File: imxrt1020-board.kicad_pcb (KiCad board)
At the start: 2 copper layers, 102.9 x 68.6 mm, 200 parts, among them J1 Micro_SD_Card_Det, J10 CASTELATED, J11 CASTELATED, J12 CASTELATED, J13 CASTELATED, J14 CASTELATED, J15 CASTELATED, J16 CASTELATED, J17 CASTELATED, J18 CASTELATED, J19 CASTELATED, J2 USB_OTG, J20 CASTELATED, J21 CASTELATED, J22 CASTELATED, J23 CASTELATED, J24 CASTELATED, J25 CASTELATED, J26 CASTELATED, J27 CASTELATED, J28 CASTELATED, J29 CASTELATED, J3 Conn_02x20_Odd_Even, J30 CASTELATED, J31 CASTELATED, J32 CASTELATED, J33 CASTELATED, J34 CASTELATED, J35 CASTELATED, J36 CASTELATED, J37 CASTELATED, J38 CASTELATED, J39 CASTELATED, J4 CASTELATED, J40 CASTELATED, J41 CASTELATED, J42 CASTELATED, J43 CASTELATED, J44 GS2, J45 GS2, J46 PWR_IN, J47 JTAG, J48 Conn_01x06, J49 CASTELATED, J5 CASTELATED, J50 CASTELATED, J51 CASTELATED, J52 CASTELATED, J53 CASTELATED, J54 CASTELATED, J55 CASTELATED, J56 CASTELATED, J57 CASTELATED, J58 SI-50196-F, J59 CASTELATED, J6 CASTELATED, J60 CASTELATED, J61 CASTELATED, J62 CASTELATED, J63 CASTELATED, J64 CASTELATED, J65 CASTELATED, J66 CASTELATED, J67 CASTELATED, J68 CASTELATED, J69 CASTELATED, J7 CASTELATED, J70 CASTELATED, J71 CASTELATED, J72 CASTELATED, J73 CASTELATED, J74 CASTELATED, J75 CASTELATED, J76 CASTELATED, J77 CASTELATED, J78 CASTELATED, J79 CASTELATED, J8 CASTELATED, J80 CASTELATED, J81 Conn_01x07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

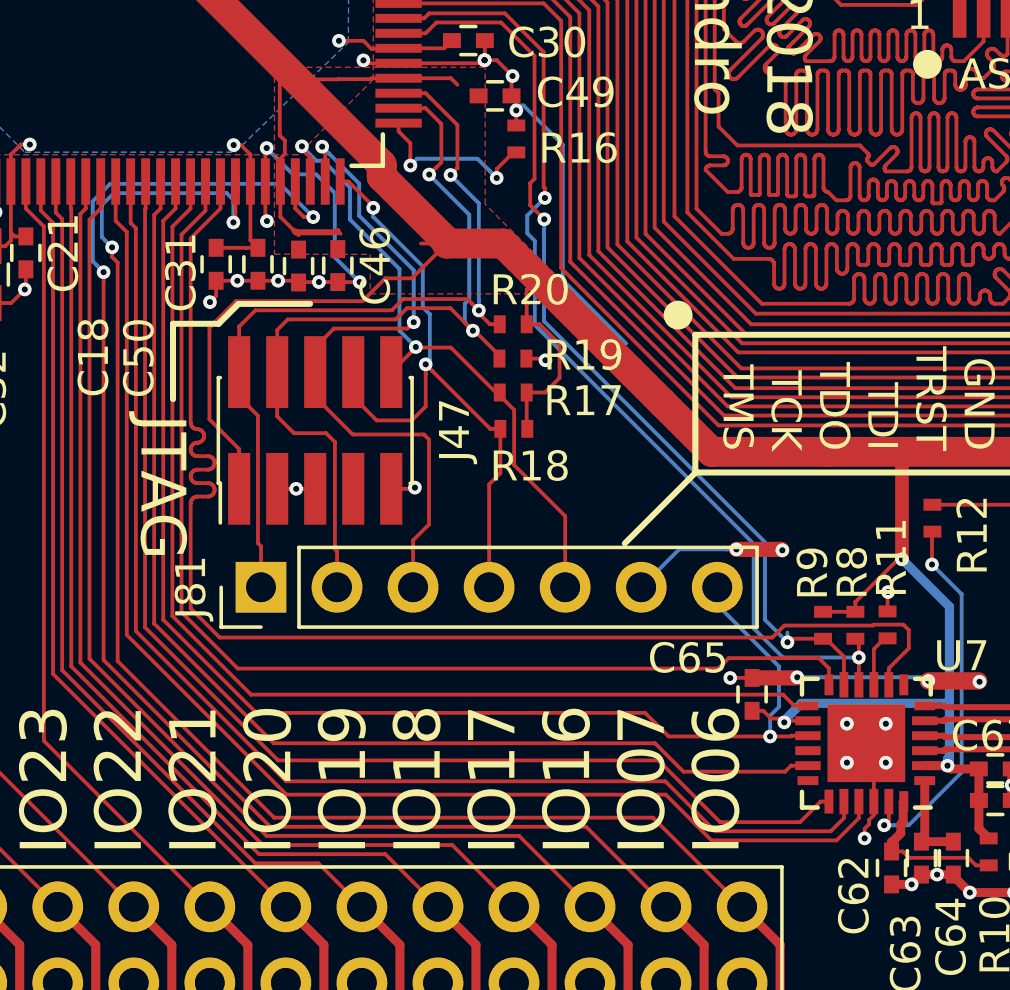
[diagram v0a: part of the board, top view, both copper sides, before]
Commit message: Tune track length of ETH data lines
Signed-off-by: Martin Ribelotta <martinribelotta@gmail.com>
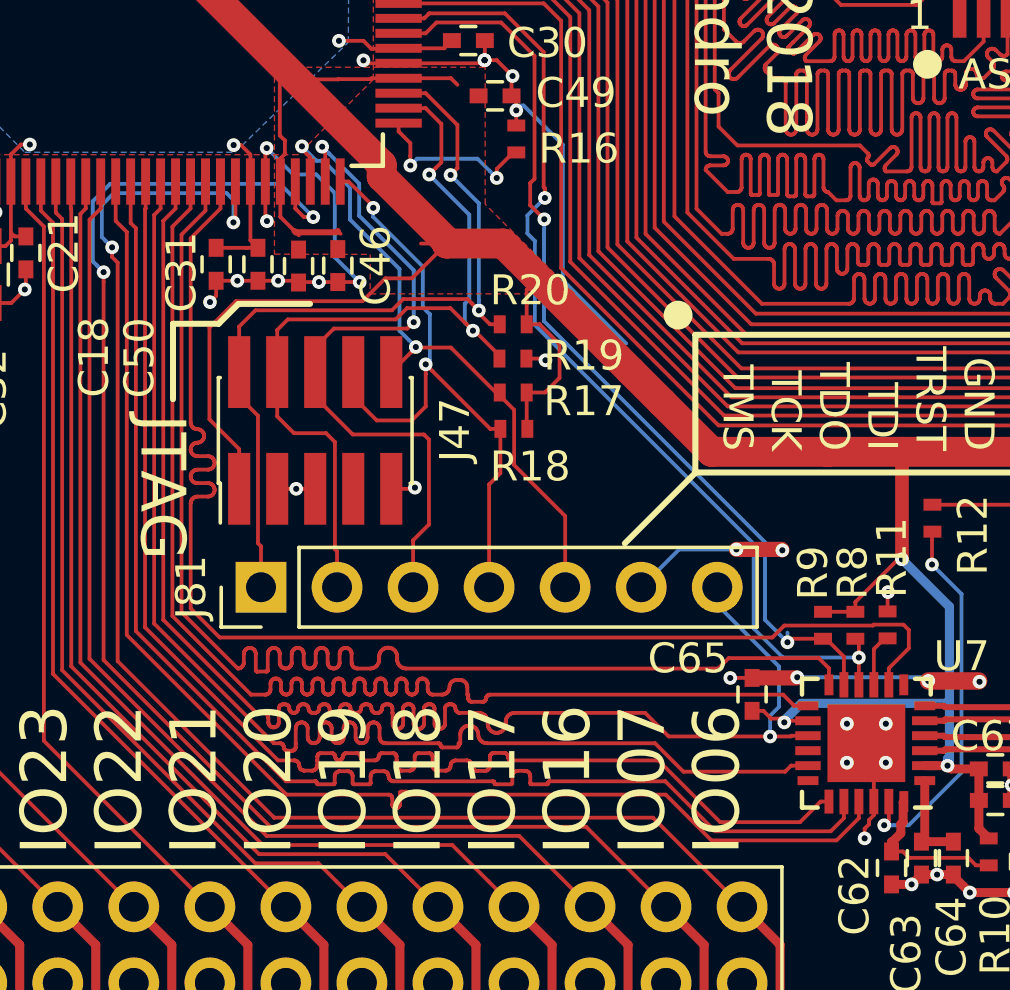
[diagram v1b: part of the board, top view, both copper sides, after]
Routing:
- net /GPIO/ENET_CRS_DV: track 43.9 -> 51.6 mm
- net /GPIO/ENET_RXD0: track 37.2 -> 44.4 mm
- net /GPIO/ENET_RXD1: track 38.0 -> 44.4 mm
- net /GPIO/ENET_RX_ER: track 38.8 -> 44.4 mm
- net /GPIO/ENET_TX_EN: track 40.7 -> 44.3 mm
- net /GPIO/ENET_TXD0: track 42.2 -> 44.3 mm
- net /GPIO/ENET_TXD1: track 43.5 -> 44.3 mm

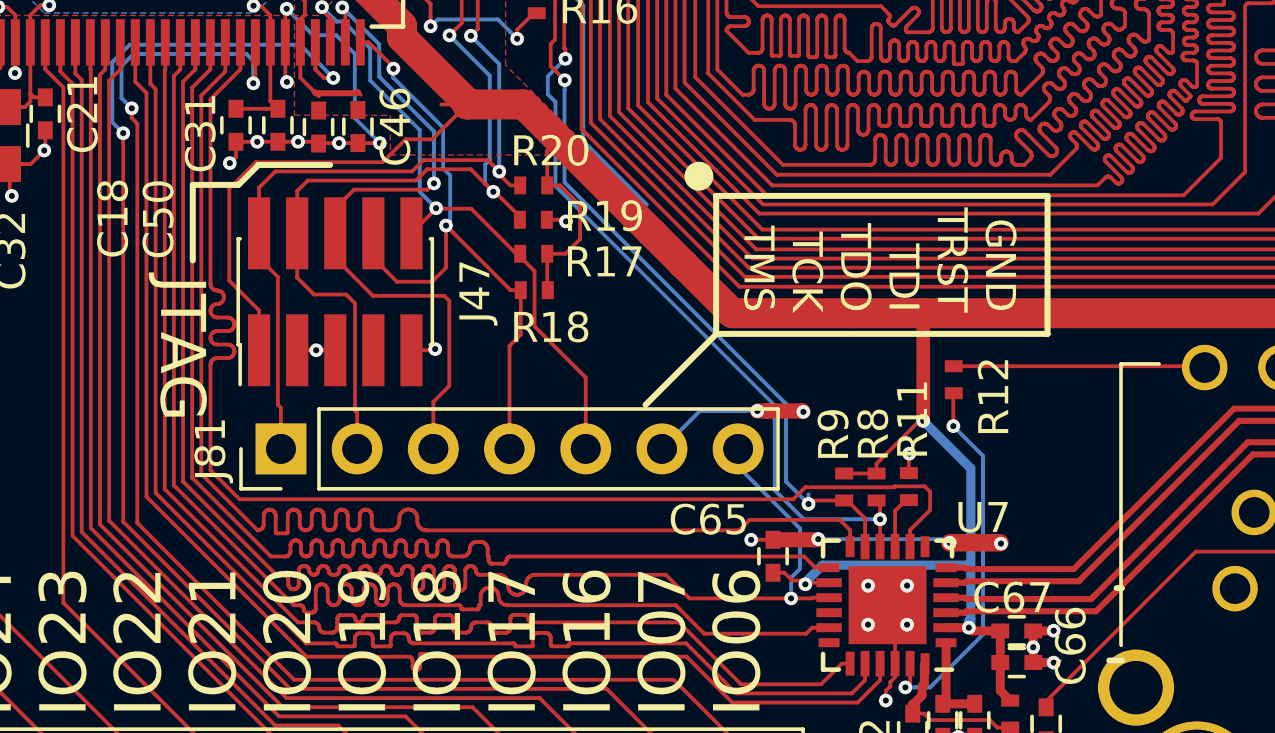
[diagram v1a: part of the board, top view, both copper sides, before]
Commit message: Update images, README.md and PCB sylkscreen for reflect the changes
Signed-off-by: Martin Ribelotta <martinribelotta@gmail.com>
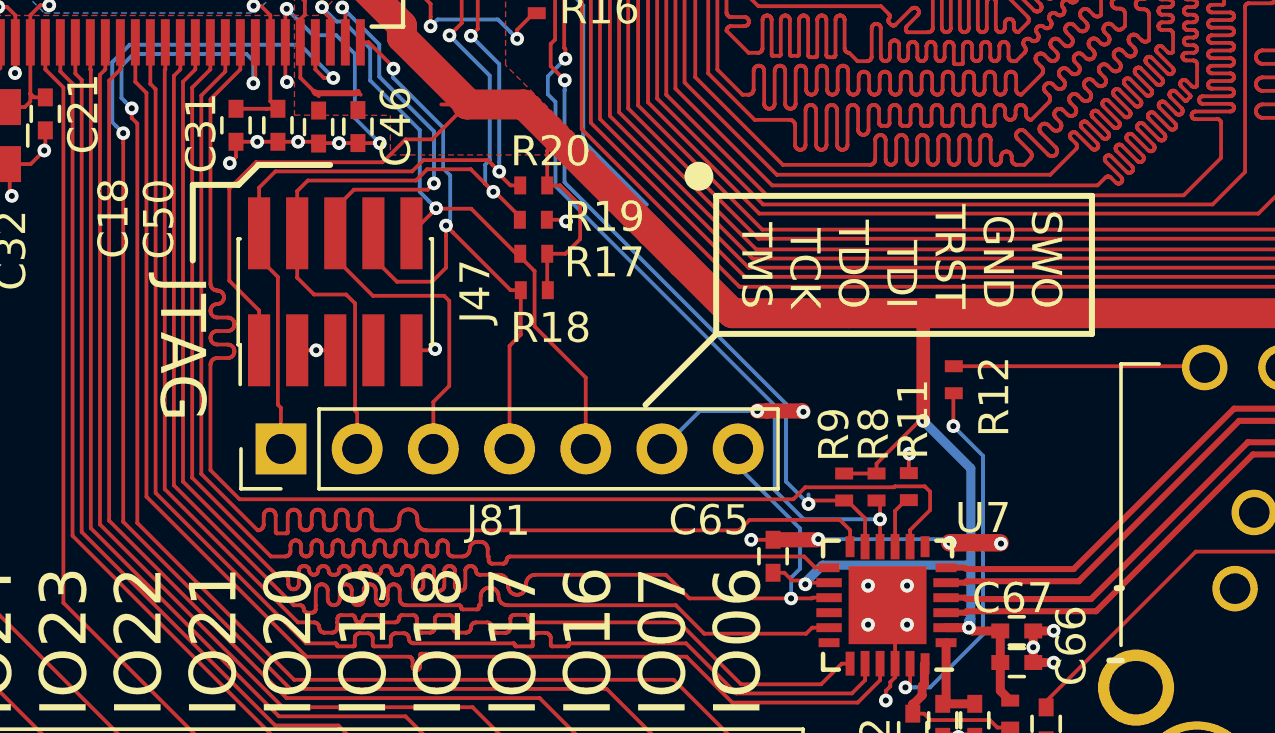
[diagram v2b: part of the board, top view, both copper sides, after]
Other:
- board text added: "SWO GND TRST TDI TDO TCK TMS"
- board text removed: "GND TRST TDI TDO TCK TMS"
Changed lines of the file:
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@@
     (descr "Through hole straight pin header, 1x07, 2.54mm pitch, single row")
     (tags "Through hole pin header THT 1x07 2.54mm single row")
-    (fp_text reference J81 (at 0 -2.33 90) (layer F.SilkS)
+    (fp_text reference J81 (at -2.4003 7.24662 180) (layer F.SilkS)
       (effects (font (size 1 1) (thickness 0.15)))
     )
@@
     (pad 7 thru_hole oval (at 0 15.24 90) (size 1.7 1.7) (drill 1) (layers *.Cu *.Mask)
       (net 87 /GPIO/ENET_CRS_DV))
-    (model ${KISYS3DMOD}/Pin_Headers.3dshapes/Pin_Header_Straight_1x07_Pitch2.54mm.wrl
-      (at (xyz 0 0 0))
-      (scale (xyz 1 1 1))
-      (rotate (xyz 0 0 0))
-    )
   )
   (gr_line (start 198.98868 81.26476) (end 206.68996 81.26476) (layer F.SilkS) (width 0.2))
@@
   (gr_line (start 174.79772 120.2436) (end 172.43298 122.60834) (layer F.SilkS) (width 0.2))
   (gr_circle (center 174.21352 114.984276) (end 174.35322 115.169696) (layer F.SilkS) (width 0.5))
-  (gr_line (start 185.83402 115.64112) (end 174.79264 115.64112) (layer F.SilkS) (width 0.2))
-  (gr_line (start 185.83402 120.24106) (end 185.83402 115.64112) (layer F.SilkS) (width 0.2))
-  (gr_line (start 174.7901 120.24106) (end 185.83402 120.24106) (layer F.SilkS) (width 0.2))
+  (gr_line (start 187.31484 115.64112) (end 174.79264 115.64112) (layer F.SilkS) (width 0.2))
+  (gr_line (start 187.31484 120.24106) (end 187.31484 115.64112) (layer F.SilkS) (width 0.2))
+  (gr_line (start 174.7901 120.24106) (end 187.31484 120.24106) (layer F.SilkS) (width 0.2))
   (gr_line (start 174.7901 115.64112) (end 174.7901 120.24106) (layer F.SilkS) (width 0.2))
-  (gr_text "GND\nTRST\nTDI\nTDO\nTCK\nTMS" (at 180.22316 119.52478 270) (layer F.SilkS)
+  (gr_text "SWO\nGND\nTRST\nTDI\nTDO\nTCK\nTMS" (at 180.95468 119.41048 270) (layer F.SilkS)
     (effects (font (size 1 1) (thickness 0.25)) (justify right))
   )

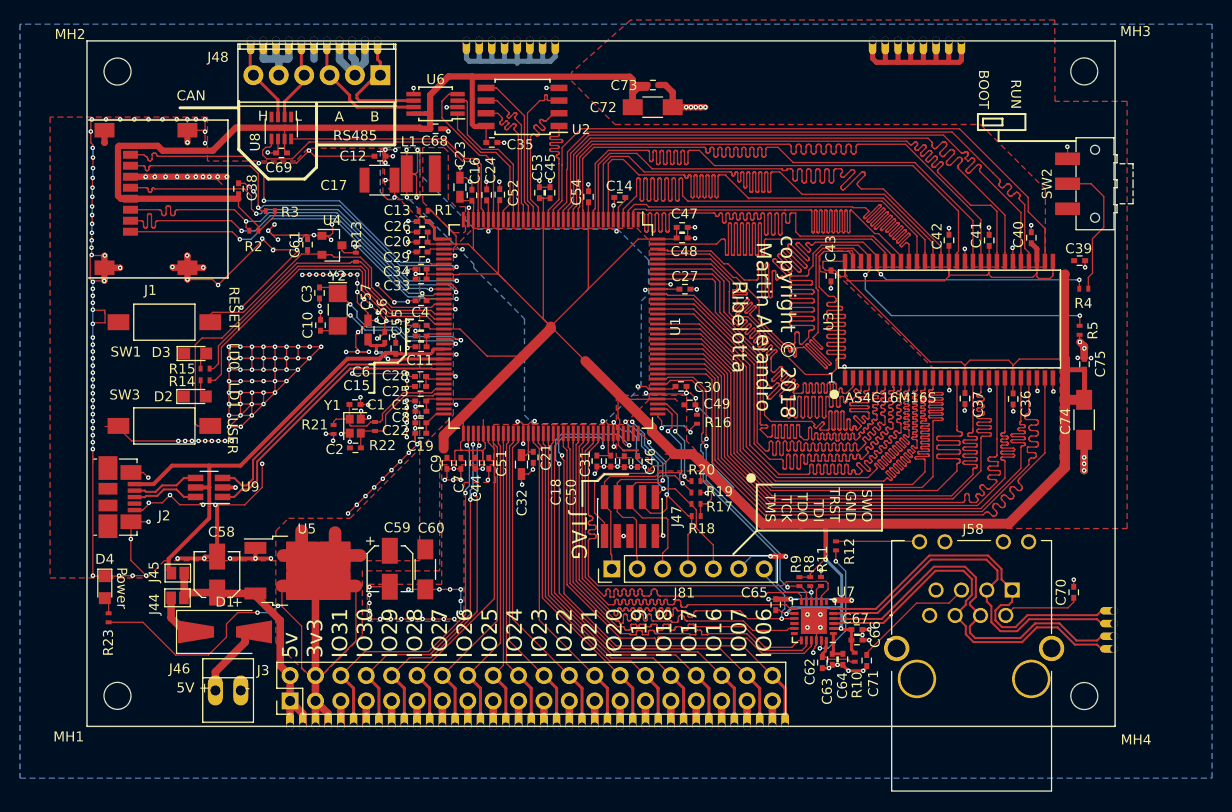
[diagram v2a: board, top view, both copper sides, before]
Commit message: First route of 6mil/6mil experiment
Signed-off-by: Martin Ribelotta <martinribelotta@gmail.com>
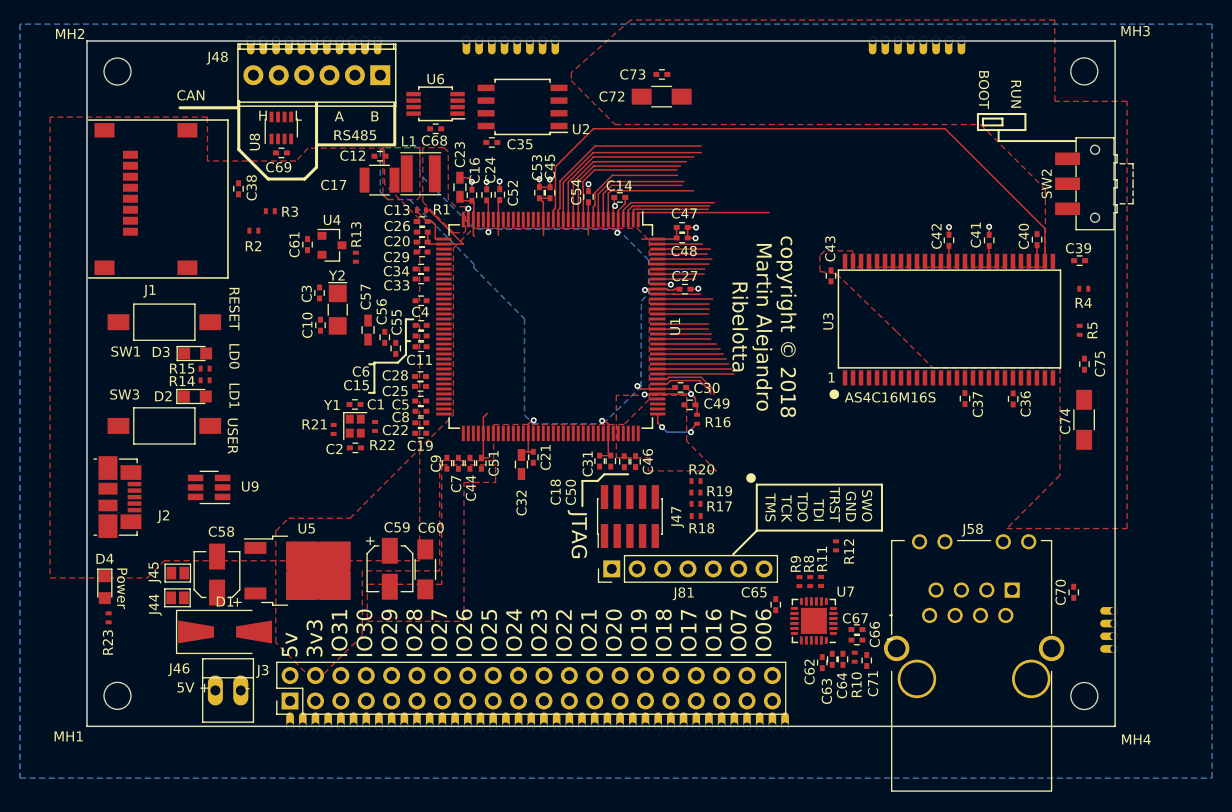
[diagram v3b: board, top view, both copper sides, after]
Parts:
- moved C72 1.38 mm to (165.3, 76.8)
- moved C73 1.38 mm to (165.3, 74.6)
- moved C51 0.75 mm to (147.2, 113.5)
- moved C40 0.60 mm to (202.8, 91.1)
- moved C44 0.49 mm to (146.1, 113.5)
- moved C31 0.28 mm to (159.1, 113.3)
- moved C7 0.25 mm to (144.9, 113.5)
- moved C46 0.19 mm to (162.7, 113.3)
- moved R1 0.18 mm to (141.2, 88.2)
- moved C30 0.11 mm to (167.2, 105.9)
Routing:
- net GND: track 620.8 -> 24.8 mm, vias 336 -> 16
- net +3V3: track 600.7 -> 41.1 mm, vias 7 -> 0
- net /MEMORY/SDRAM_A1: track 91.5 -> 4.96 mm, vias 2 -> 0
- net /MEMORY/SDRAM_A0: track 87.4 -> 5.27 mm, vias 2 -> 0
- net /MEMORY/SDRAM_A6: track 64.9 -> 3.74 mm
- net /MEMORY/SDRAM_A7: track 64.9 -> 4.30 mm
- net /MEMORY/SDRAM_A10: track 64.9 -> 4.46 mm
- net /MEMORY/SDRAM_A5: track 64.9 -> 4.64 mm
- net /MEMORY/SDRAM_A4: track 64.9 -> 4.72 mm
- net /MEMORY/SDRAM_CLK: track 64.9 -> 5.07 mm
- net /MEMORY/SDRAM_CKE: track 64.9 -> 5.08 mm
- net /MEMORY/SDRAM_A12: track 64.9 -> 5.08 mm
- net /MEMORY/SDRAM_A9: track 64.9 -> 5.15 mm
- net /MEMORY/SDRAM_A11: track 64.9 -> 5.15 mm
- net /MEMORY/SDRAM_Q8: track 64.9 -> 5.31 mm
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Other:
- net class Default: trace_width 0.127 -> 0.1524; via_dia 0.4572 -> 0.6; via_drill 0.2032 -> 0.3
- rule trace_min: 0.127 -> 0.1524
- rule via_min_drill: 0.2032 -> 0.3
- rule via_min_size: 0.4572 -> 0.6

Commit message: Save commit after kicad-5 migration
Signed-off-by: Martin Ribelotta <martinribelotta@gmail.com>
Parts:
- moved R5 23.0 mm to (186.0, 91.2), turned to 90 degrees
- moved R2 2.38 mm to (124.6, 87.9), turned to 0 degrees
- moved R3 2.28 mm to (124.5, 86.6), turned to 0 degrees
- moved R22 0.57 mm to (137.1, 109.5)
- moved C16 0.24 mm to (146.3, 86.4)
- moved C23 0.24 mm to (145.1, 85.6)
- moved C43 0.08 mm to (182.1, 94.7)
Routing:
- net /MEMORY/SDRAM_CLK: track 5.07 -> 61.2 mm
- net /MEMORY/SDRAM_A12: track 5.08 -> 61.1 mm
- net /MEMORY/SDRAM_CKE: track 5.08 -> 61.1 mm
- net /MEMORY/SDRAM_A11: track 5.15 -> 61.1 mm
- net /MEMORY/SDRAM_Q15: track 7.63 -> 55.3 mm
- net /MEMORY/SDRAM_Q14: track 7.36 -> 54.0 mm
- net /MEMORY/SDRAM_Q13: track 7.10 -> 53.1 mm
- net /MEMORY/SDRAM_A0: track 5.27 -> 49.9 mm, vias 0 -> 2
- net /MEMORY/SDRAM_Q12: track 6.85 -> 51.2 mm
- net GND: track 24.8 -> 69.0 mm, vias 16 -> 57
- net /MEMORY/SDRAM_Q11: track 6.56 -> 50.2 mm
- net /MEMORY/SDRAM_Q10: track 6.24 -> 48.9 mm
- net /MEMORY/SDRAM_Q9: track 5.85 -> 47.4 mm
- net /MEMORY/SDRAM_Q8: track 5.31 -> 45.3 mm
- net /MEMORY/SDRAM_Q1: track 19.5 -> 58.7 mm
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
